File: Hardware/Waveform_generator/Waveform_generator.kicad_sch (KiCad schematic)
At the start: 104 parts, among them J1 Conn_01x02, J2 Conn_01x02, J3 Conn_01x02, J4 Conn_01x02, SW1 SW_DPDT_x2, U1 TPS54202DDC, U10 MCP4822, U11 LM1875, U12 OPA549T, U2 TL072, U3 ESP32-DEVKITC-32U, U4 TSR1-2450E, U5 XC6206PxxxMR, U6 AD9837BCPZ-RL7, U7 TL072, U8 AD5160, U9 TL072, Y1 X1G0041710027

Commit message: Rellenado archivo Config y desarrollada la UI web
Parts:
- removed C29, C31: 100nF, Capacitor_SMD:C_0603_1608Metric_Pad1.08x0.95mm_HandSolder, symbol Device:C
- removed C30, C32: 10uF, Capacitor_Tantalum_SMD:CP_EIA-3216-18_Kemet-A_HandSolder, symbol Device:C_Polarized
- removed D6, D7: D, Diode_THT:D_DO-41_SOD81_P10.16mm_Horizontal, symbol Device:D
- removed R27: 3k, Resistor_SMD:R_0805_2012Metric_Pad1.20x1.40mm_HandSolder, symbol Device:R
- removed R28: 47k, Resistor_SMD:R_0805_2012Metric_Pad1.20x1.40mm_HandSolder, symbol Device:R
- removed R29: 4k99, Resistor_SMD:R_0805_2012Metric_Pad1.20x1.40mm_HandSolder, symbol Device:R
- removed R30: 10k, Resistor_SMD:R_0805_2012Metric_Pad1.20x1.40mm_HandSolder, symbol Device:R
- removed TP13: ${FAMILY}, HARWIN SMD:HARWIN_S1751-46, symbol CERN:HARWIN/HARWIN_S1751-46
- removed U12: OPA549T, footprints:OPA549T, symbol SpecialSymbols:OPA549T

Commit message: Revisión 1 del hardware. Reorganizaco un poco el layout y añadidos shottky de protección, puente para desconectar el buck, conectores de pogo para conectar a masa la carcasa de aluminio, agrandado el espacio del powerOpAmp para un mayor disipador...
Actualizado el controlador para que por USB no printee la batería todo el rato.

Añadida opción de reseteo del AD9837 en cada comando para probar si se soluciona el problema  (no genera nada a la salida)
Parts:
- added D6: SS34, Diode_SMD:D_SMA, symbol Diode:SS34
- added H1: MountingHole_Pad, MountingHole:MountingHole_3.2mm_M3_Pad_TopBottom, symbol Mechanical:MountingHole_Pad
- added J5, J6: PogoPin, CUSTOM:Pogo pin 1x3 2.54mm male horizontal, symbol Connector:Conn_01x03_Pin
- added J7: GND_CHASIS, Connector_PinHeader_2.54mm:PinHeader_1x03_P2.54mm_Vertical, symbol Connector:Conn_01x03_Pin
- added J8: GND_CHASIS, Connector_PinHeader_2.54mm:PinHeader_1x02_P2.54mm_Vertical, symbol Connector:Conn_01x02_Pin
- added R32: 0R, Resistor_SMD:R_0805_2012Metric_Pad1.20x1.40mm_HandSolder, symbol Device:R
- added TP13: TP, TestPoint:TestPoint_THTPad_D2.0mm_Drill1.0mm, symbol Connector:TestPoint
- added TP15: Buck out, TestPoint:TestPoint_THTPad_D2.0mm_Drill1.0mm, symbol Connector:TestPoint
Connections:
- net +12V: now also R32.1; no longer C1.1, C2.1, U1.3 (VIN)
- net +12V_IN: now also SW1.3 (C); no longer SW1.1 (A)
- net +3V3: now also Y1.1 (~{ST})
- net +5V: now also D6.1 (K); no longer C5.1, C6.1, L1.2, R7.2, U4.3 (Vout)
- net -12V_IN: now also SW1.4 (A); no longer SW1.6 (C)
- net GND: now also H1.1, J7.3 (Pin_3), J8.1 (Pin_1)
- new net 12V_buck: C1.1, C2.1, R32.2, U1.3 (VIN)
- new net 5V_buck: C5.1, C6.1, D6.2 (A), L1.2, R7.2, TP15.1, U4.3 (Vout)
- new net GNDS: J5.1 (Pin_1), J5.2 (Pin_2), J5.3 (Pin_3), J7.2 (Pin_2), TP13.1
- new net GNDS1: J6.1 (Pin_1), J6.2 (Pin_2), J6.3 (Pin_3), J8.2 (Pin_2)
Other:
- moved on the sheet: C1, C11, C12, C17, C18, C19, C2, C20, C3, C4, C5, C6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

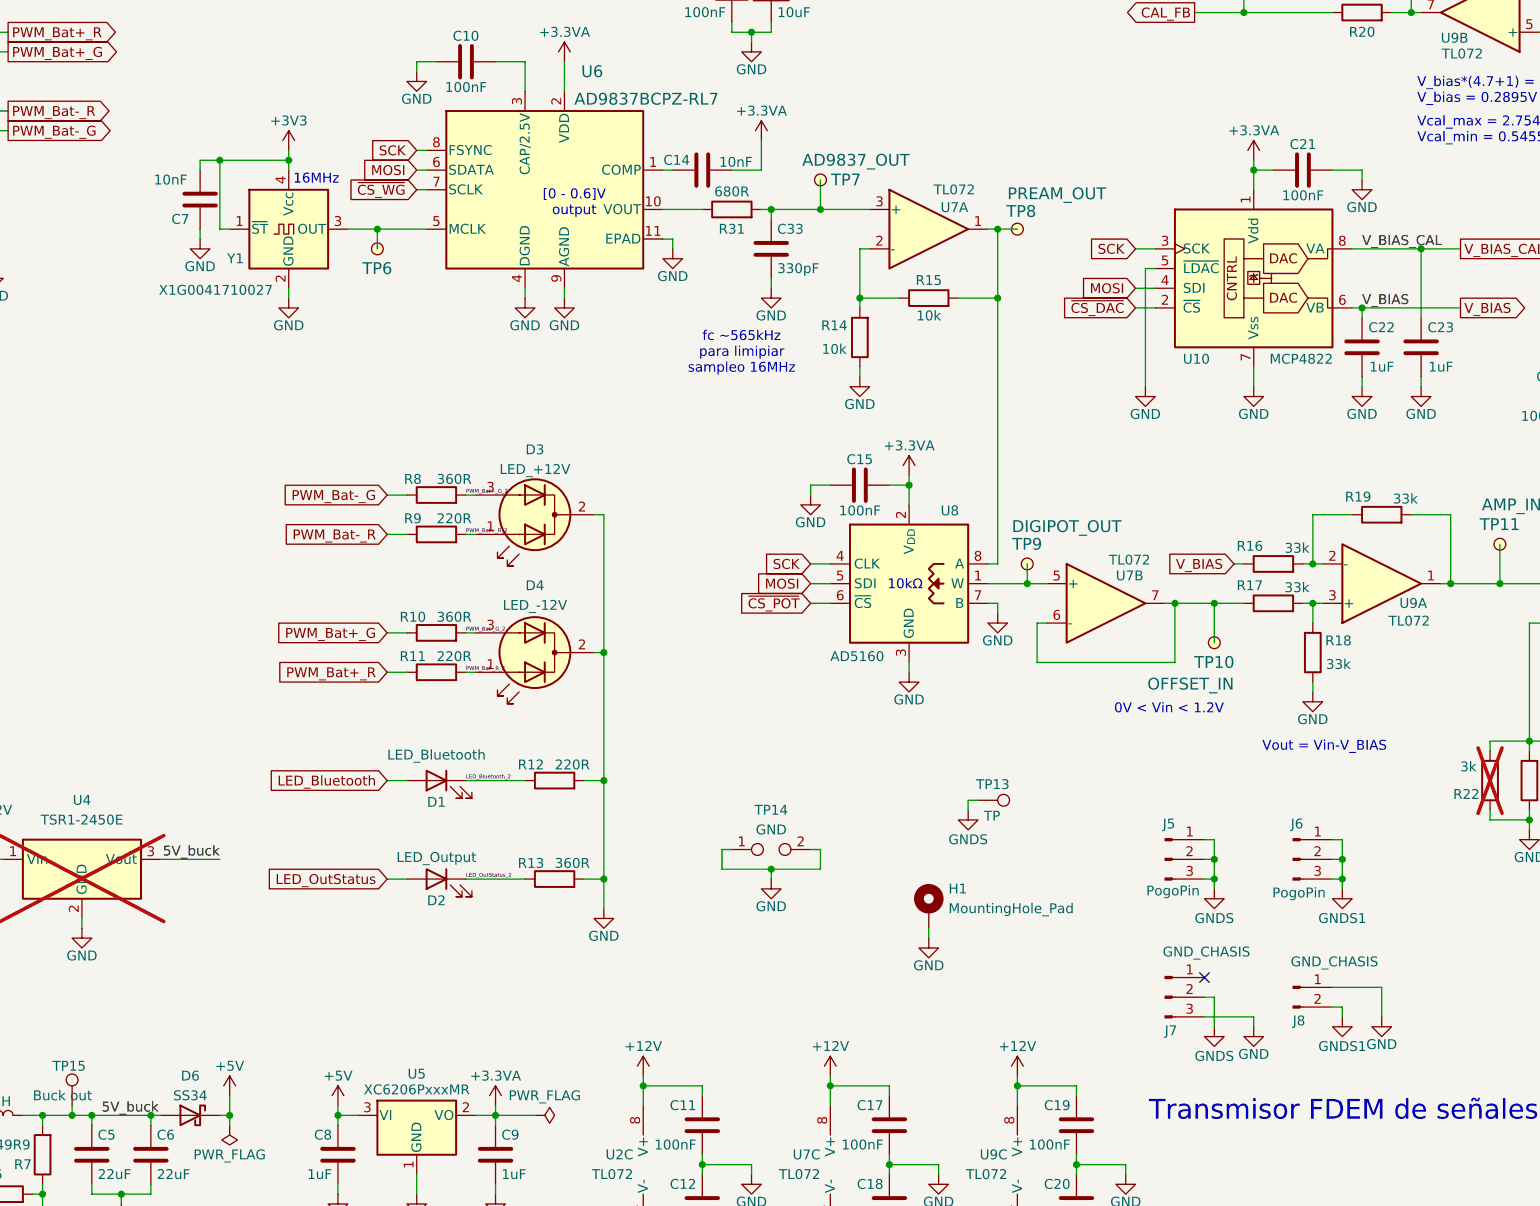
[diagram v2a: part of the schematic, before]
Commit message: Rev 2 de hardware actualizada con error en los pines del ad9837 (SCLK y CS intercambiados). ERROR IDENTIFICADO
Añadida corrección del offset que hay a la salida del ad9837 que antes no se tenía en cuenta.
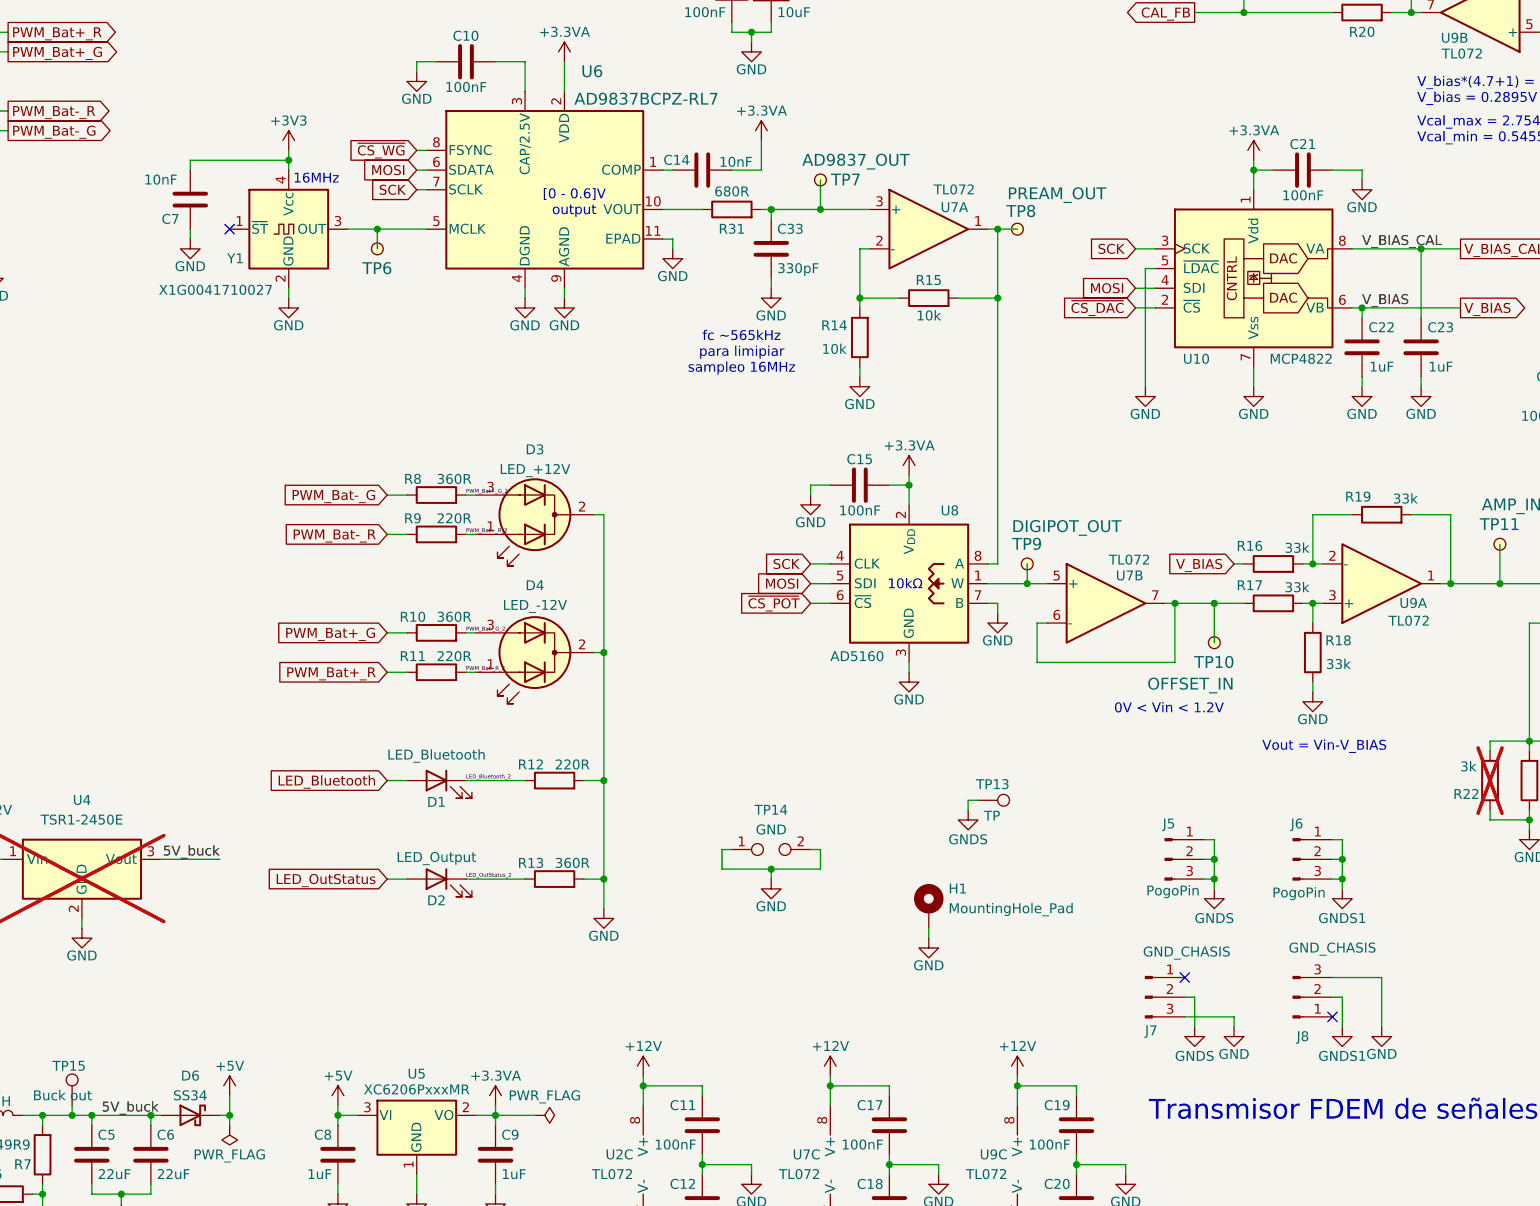
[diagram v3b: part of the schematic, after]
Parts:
- removed J8: GND_CHASIS, Connector_PinHeader_2.54mm:PinHeader_1x02_P2.54mm_Vertical, symbol Connector:Conn_01x02_Pin
- added J8: GND_CHASIS, Connector_PinHeader_2.54mm:PinHeader_1x03_P2.54mm_Horizontal, symbol Connector:Conn_01x03_Pin
- R32: footprint Resistor_SMD:R_0805_2012Metric_Pad1.20x1.40mm_HandSolder -> Resistor_SMD:R_1206_3216Metric_Pad1.30x1.75mm_HandSolder
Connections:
- net +3V3: no longer Y1.1 (~{ST})
- net GND: now also J8.3 (Pin_3)
- net GNDS1: now also J8.2 (Pin_2)
- net SCK: now also U6.7 (SCLK); no longer U6.8 (FSYNC)
- net ~{CS_WG}: now also U6.8 (FSYNC); no longer U6.7 (SCLK)
- no-connect marks 23 -> 25
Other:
- moved on the sheet: C7, J7
